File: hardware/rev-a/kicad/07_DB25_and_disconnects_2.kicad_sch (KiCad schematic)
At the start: 2 parts, among them J5 DMR-25SGG DB25F, J6 Intensity external driver

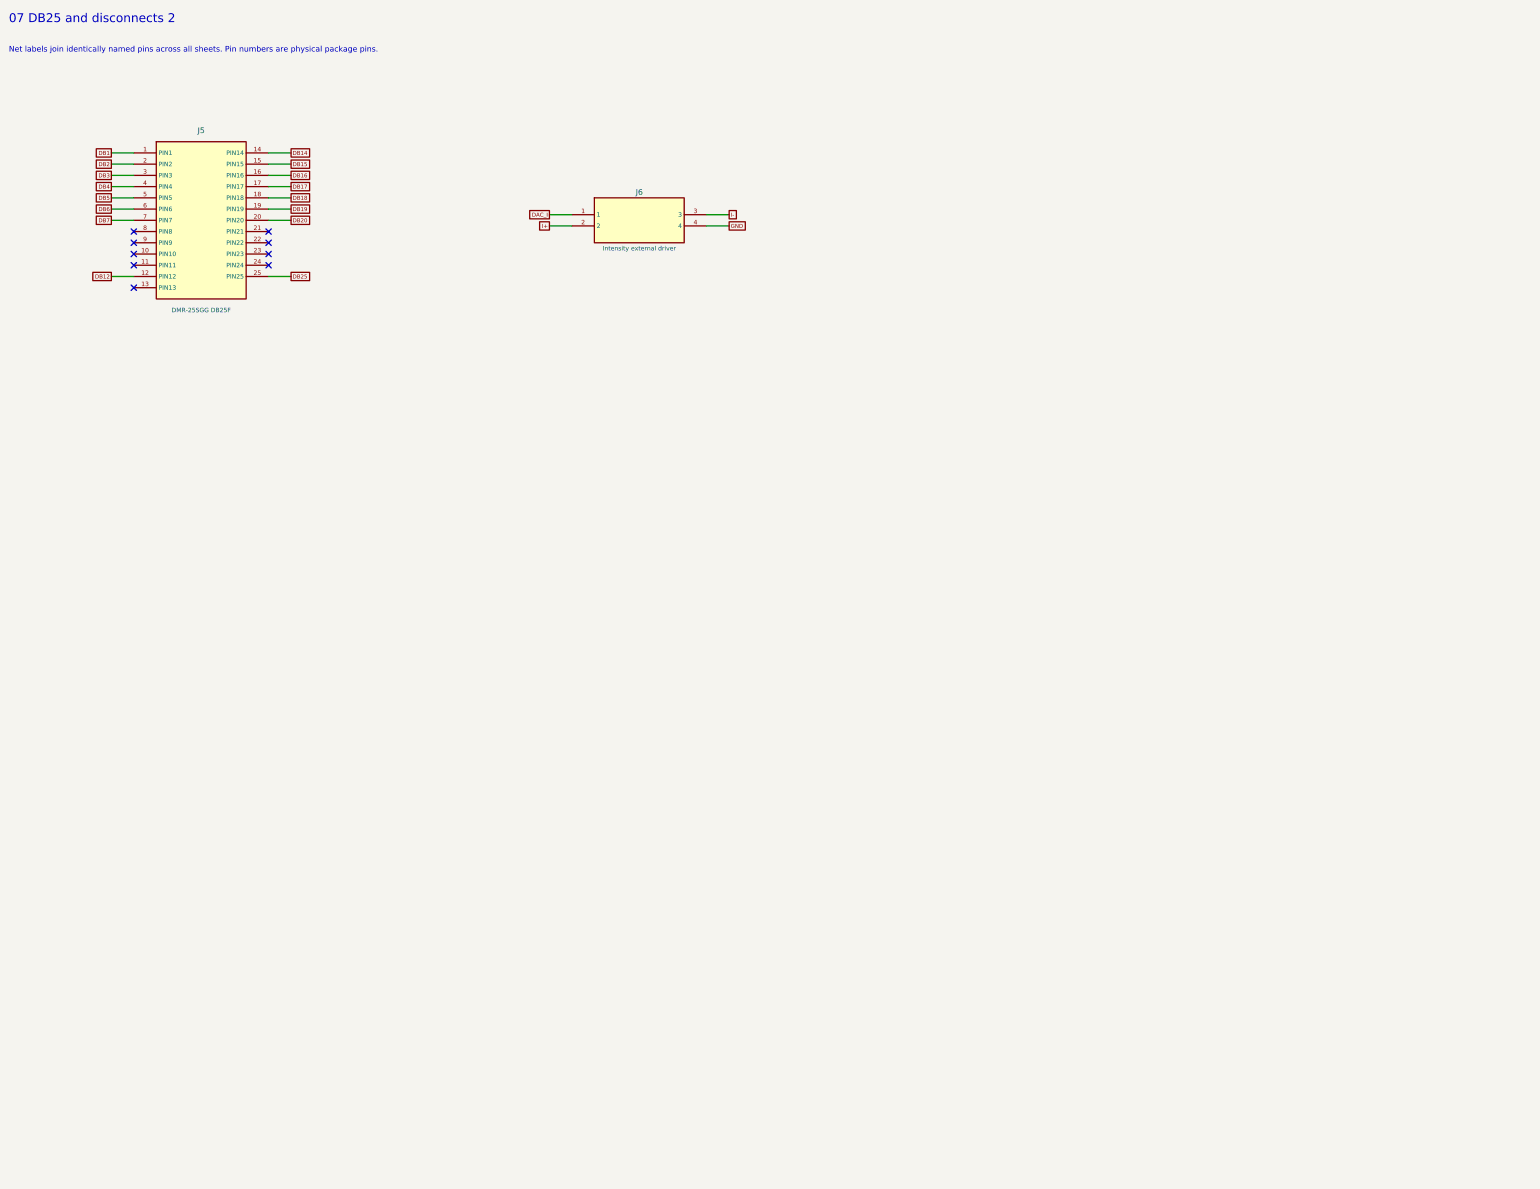
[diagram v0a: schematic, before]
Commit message: Redraw Rev.A schematics with functional blocks and explicit wiring
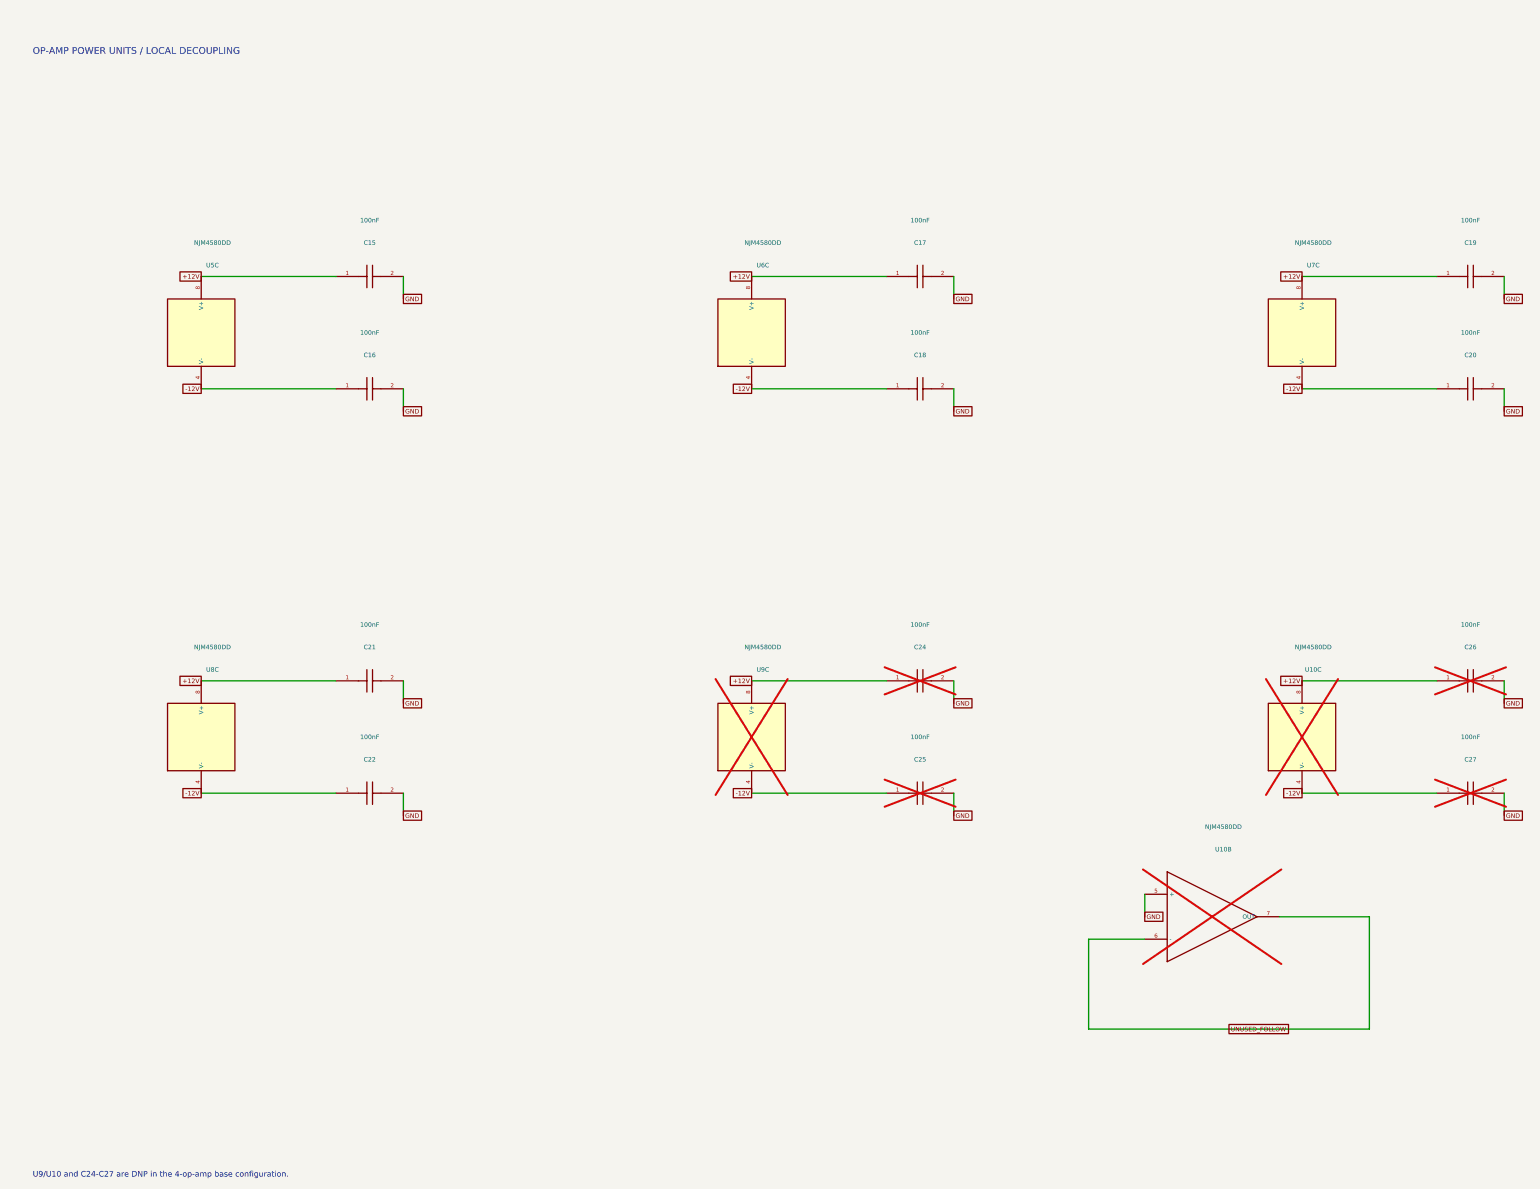
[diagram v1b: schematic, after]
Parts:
- removed J5: DMR-25SGG DB25F, RevA:DMR25SGG, symbol RevA:DB25_J5
- removed J6: Intensity external driver, RevA:PinHeader_1x04_P2.54mm_Vertical, symbol RevA:Conn_J6
- added C15, C16, C17, C18, C19, C20, C21, C22, C24, C25, C26, C27: 100nF, RevA:C_Disc_D5.0mm_W2.5mm_P5.00mm, symbol RevA:C
- added U10, U5, U6, U7, U8, U9: NJM4580DD, RevA:DIP-8_W7.62mm, symbol RevA:AMP
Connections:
- net GND: now also C15.2, C16.2, C17.2, C18.2, C19.2, C20.2, C21.2, C22.2, C24.2, C25.2, C26.2, C27.2, U10.5 (+)
- new net +12V: C15.1, C17.1, C19.1, C21.1, C24.1, C26.1, U10.8 (V+), U5.8 (V+), U6.8 (V+), U7.8 (V+), U8.8 (V+), U9.8 (V+)
- new net -12V: C16.1, C18.1, C20.1, C22.1, C25.1, C27.1, U10.4 (V-), U5.4 (V-), U6.4 (V-), U7.4 (V-), U8.4 (V-), U9.4 (V-)
- new net UNUSED_FOLLOW: U10.6 (-), U10.7 (OUT)
- no-connect marks 9 -> 0
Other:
- note added: "OP-AMP POWER UNITS / LOCAL DECOUPLING"
- note added: "U9/U10 and C24-C27 are DNP in the 4-op-amp base configuration."
- note removed: "07 DB25 and disconnects 2"
- note removed: "Net labels join identically named pins across all sheets. Pin numbers are physical package pins."
- company: CoreS3 ILDA evaluation -> (none)
- title: 07_DB25_and_disconnects_2 -> 13 / Op-amp power and unused section
